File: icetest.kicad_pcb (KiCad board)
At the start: 2 copper layers, 66.7 x 57.2 mm, 57 parts, among them J1 R, J2 R, J3 R

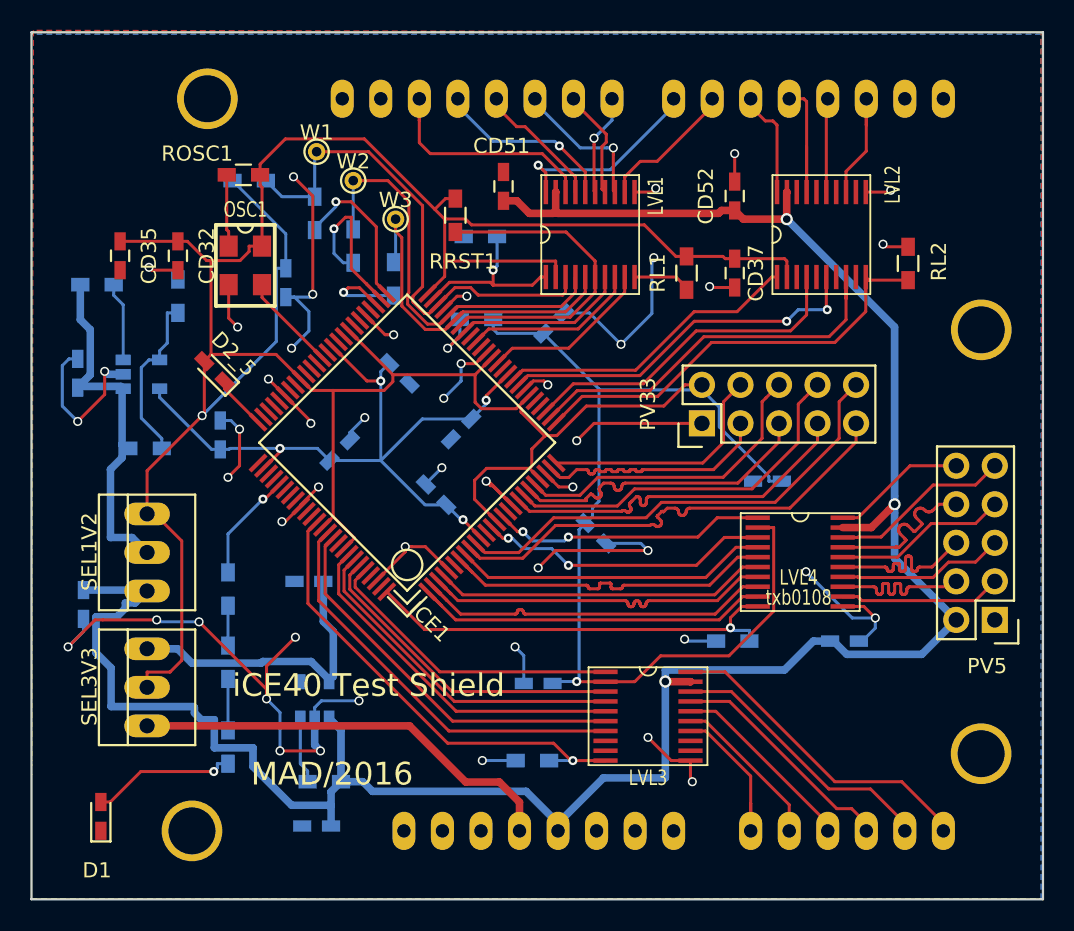
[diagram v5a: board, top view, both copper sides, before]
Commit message: add LED2 and update layout
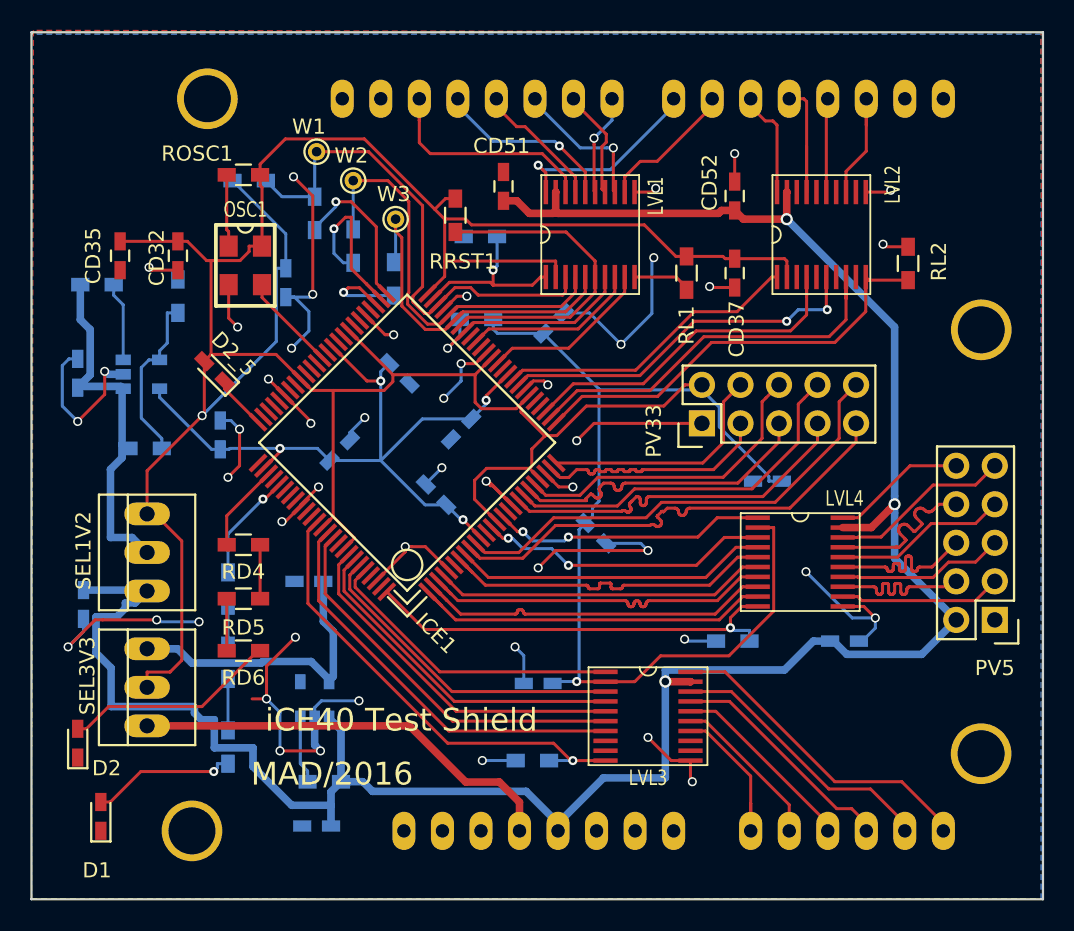
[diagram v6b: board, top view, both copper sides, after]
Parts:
- added D2: LED, local:D_0603_HandSoldering, F.Cu at (126.2, 140.2)
- added RD4: 22, Resistors_SMD:R_0603_HandSoldering, F.Cu at (137.2, 127.1)
- added RD5: 22, Resistors_SMD:R_0603_HandSoldering, F.Cu at (137.2, 130.7)
- added RD6: 22, Resistors_SMD:R_0603_HandSoldering, F.Cu at (137.2, 134.1)
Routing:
- net Net-(D2-Pad2): track 0.00 -> 14.2 mm
- net GND: track 168.5 -> 162.6 mm
- net Net-(ICE1-Pad78): track 0.00 -> 5.83 mm
- net Net-(RD4-Pad2): track 0.00 -> 3.56 mm
- net Net-(RD5-Pad2): track 0.00 -> 3.43 mm

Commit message: clean and oshpart rules
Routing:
- net GND: track 162.6 -> 178.2 mm, vias 48 -> 50
- net Net-(ICE1-Pad52): track 12.2 -> 8.57 mm
- net +3V3: track 261.0 -> 264.5 mm
- net /Arduino Shield/LOG_L3E: track 31.1 -> 32.1 mm
- net /Arduino Shield/ANA2: track 23.7 -> 24.7 mm
- net /Arduino Shield/ANA0: track 27.6 -> 28.6 mm
- net /Arduino Shield/ANA1: track 26.2 -> 27.0 mm
- net /Arduino Shield/DIG5: track 20.2 -> 20.9 mm
- net /Arduino Shield/ANA3: track 23.0 -> 23.6 mm
- net /Arduino Shield/MOSI: track 27.7 -> 28.3 mm
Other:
- net class Default: clearance 0.152 -> 0.1524; trace_width 0.2 -> 0.1778; via_dia 0.6 -> 0.5588; via_drill 0.4 -> 0.381
- net class Ground: clearance 0.152 -> 0.1524; trace_width 0.2 -> 0.1778; via_dia 0.6 -> 0.5588; via_drill 0.4 -> 0.381
- net class Power: clearance 0.2 -> 0.2032; trace_width 0.5 -> 0.3556; via_dia 0.8 -> 0.762; via_drill 0.5 -> 0.4826
- rule trace_clearance: 0.152 -> 0.1524
- rule trace_min: 0.152 -> 0.1524
- rule via_min_drill: 0.33 -> 0.3302
- rule via_min_size: 0.5 -> 0.508

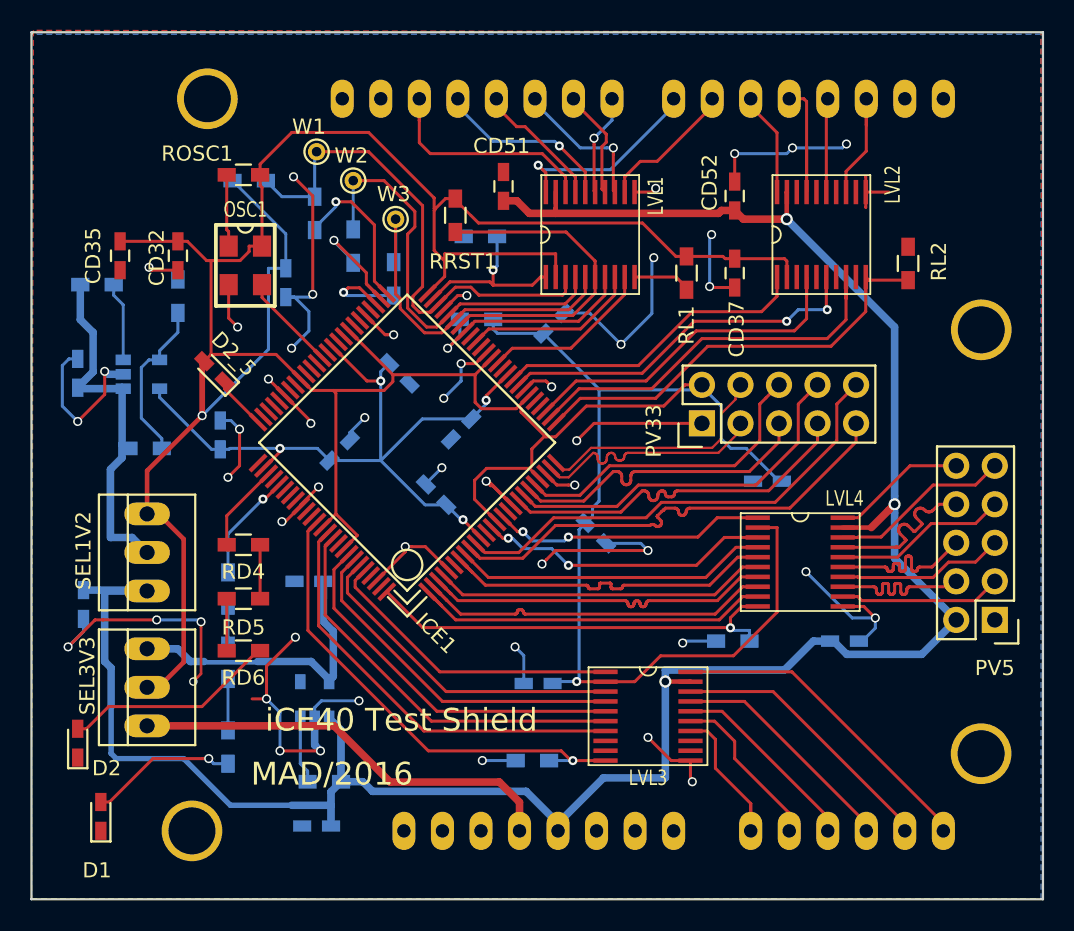
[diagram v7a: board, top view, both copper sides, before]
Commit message: fix solder mask gap and others
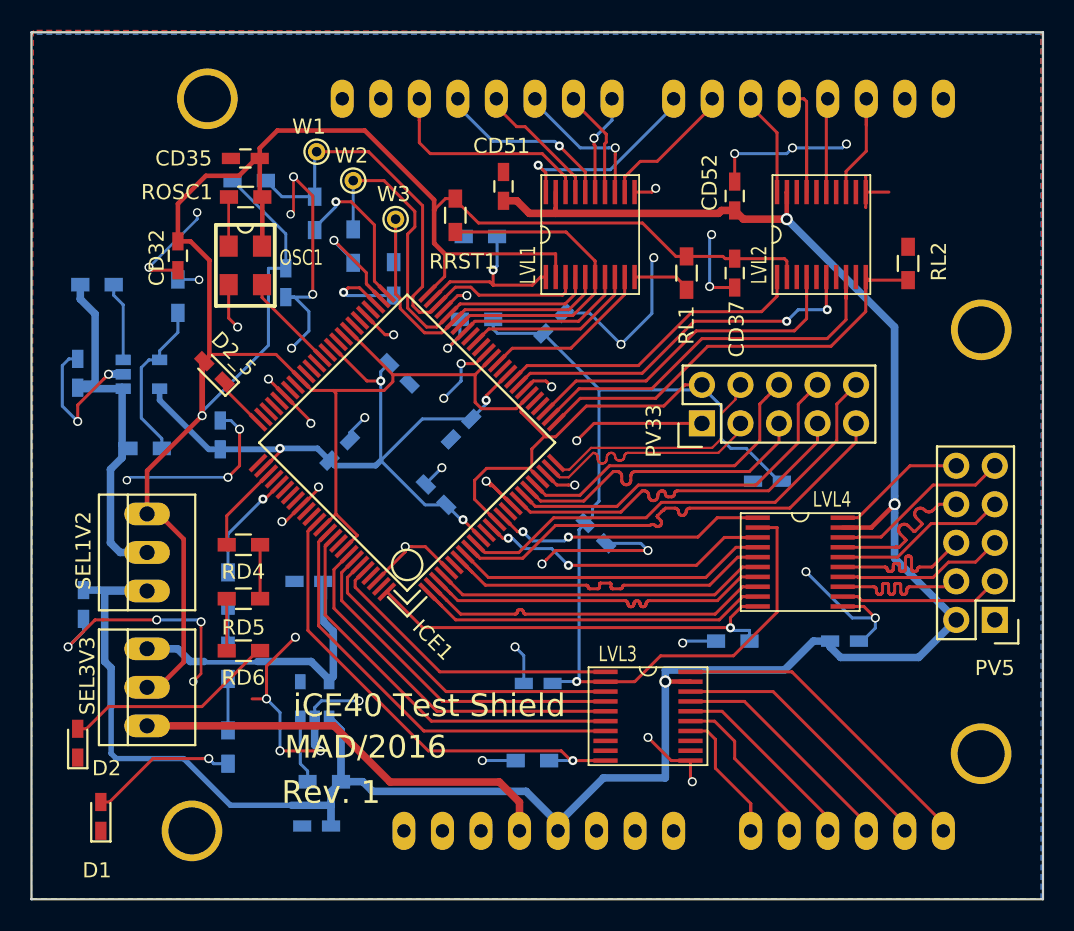
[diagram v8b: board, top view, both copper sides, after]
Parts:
- moved CD35 10.5 mm to (137.3, 101.7), turned to 180 degrees
- moved ROSC1 1.47 mm to (137.3, 104.2)
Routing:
- net GND: track 178.2 -> 193.5 mm, vias 50 -> 54
- net +3V3: track 264.5 -> 266.8 mm
- net Net-(OSC1-Pad1): track 4.75 -> 3.25 mm
- net /iVcc: track 23.7 -> 24.6 mm
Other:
- board text added: "Rev. 1"
